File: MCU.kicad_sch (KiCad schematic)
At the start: 33 parts, among them J1 Conn_ARM_SWD_TagConnect_TC2030, U1 STM32WB55CGUx, U2 FM24CL16B, U3 MLPF-WB55-01E3, X1 32MHz, X2 32kHz768

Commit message: Added test points and other cleanup
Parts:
- C14, C15: value C -> 10pF
- TP1, TP2: footprint (none) -> TestPoint:TestPoint_Pad_D1.0mm
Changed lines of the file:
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@@
 	)
 	(junction
+		(at 36.83 31.75)
+		(diameter 0)
+		(color 0 0 0 0)
+	)
+	(junction
 		(at 78.74 21.59)
 		(diameter 0)
@@
 	)
 	(junction
-		(at 101.6 67.31)
-		(diameter 0)
-		(color 0 0 0 0)
-	)
-	(junction
-		(at 34.29 31.75)
-		(diameter 0)
-		(color 0 0 0 0)
-	)
-	(junction
 		(at 133.35 49.53)
 		(diameter 0)
@@
 	)
 	(junction
-		(at 138.43 142.24)
+		(at 101.6 67.31)
 		(diameter 0)
 		(color 0 0 0 0)
 	)
 	(junction
-		(at 106.68 106.68)
+		(at 138.43 142.24)
 		(diameter 0)
 		(color 0 0 0 0)
 	)
 	(junction
-		(at 45.72 21.59)
+		(at 106.68 106.68)
 		(diameter 0)
 		(color 0 0 0 0)
@@
 	(wire
 		(pts
-			(xy 40.64 21.59) (xy 45.72 21.59)
-		)
-		(stroke
-			(width 0)
-			(type default)
-		)
-	)
-	(wire
-		(pts
-			(xy 69.85 69.85) (xy 115.57 69.85)
+			(xy 36.83 31.75) (xy 40.64 31.75)
 		)
 		(stroke
@@
 	(wire
 		(pts
-			(xy 101.6 67.31) (xy 115.57 67.31)
+			(xy 40.64 21.59) (xy 53.34 21.59)
 		)
 		(stroke
@@
 	(wire
 		(pts
-			(xy 45.72 21.59) (xy 53.34 21.59)
+			(xy 130.81 49.53) (xy 124.46 49.53)
 		)
 		(stroke
@@
 	(wire
 		(pts
-			(xy 130.81 49.53) (xy 124.46 49.53)
+			(xy 106.68 106.68) (xy 106.68 109.22)
 		)
 		(stroke
@@
 	(wire
 		(pts
-			(xy 106.68 106.68) (xy 106.68 109.22)
+			(xy 161.29 95.25) (xy 208.28 95.25)
 		)
 		(stroke
@@
 	(wire
 		(pts
-			(xy 161.29 95.25) (xy 208.28 95.25)
+			(xy 163.83 39.37) (xy 163.83 38.1)
 		)
 		(stroke
@@
 	(wire
 		(pts
-			(xy 163.83 39.37) (xy 163.83 38.1)
+			(xy 27.94 20.32) (xy 27.94 21.59)
 		)
 		(stroke
@@
 	(wire
 		(pts
-			(xy 27.94 20.32) (xy 27.94 21.59)
+			(xy 161.29 123.19) (xy 171.45 123.19)
 		)
 		(stroke
@@
 	(wire
 		(pts
-			(xy 161.29 123.19) (xy 171.45 123.19)
+			(xy 46.99 107.95) (xy 46.99 116.84)
 		)
 		(stroke
@@
 	(wire
 		(pts
-			(xy 46.99 107.95) (xy 46.99 116.84)
+			(xy 101.6 67.31) (xy 115.57 67.31)
 		)
 		(stroke
@@
 	(wire
 		(pts
-			(xy 27.94 31.75) (xy 34.29 31.75)
+			(xy 27.94 31.75) (xy 36.83 31.75)
 		)
 		(stroke
@@
 	(wire
 		(pts
-			(xy 34.29 31.75) (xy 40.64 31.75)
-		)
-		(stroke
-			(width 0)
-			(type default)
-		)
-	)
-	(wire
-		(pts
 			(xy 27.94 21.59) (xy 40.64 21.59)
 		)
@@
 	(wire
 		(pts
+			(xy 69.85 69.85) (xy 115.57 69.85)
+		)
+		(stroke
+			(width 0)
+			(type default)
+		)
+	)
+	(wire
+		(pts
 			(xy 138.43 135.89) (xy 138.43 142.24)
 		)
@@
 	)
 	(symbol
-		(lib_id "power:PWR_FLAG")
-		(at 45.72 21.59 0)
-		(unit 1)
-		(exclude_from_sim no)
-		(in_bom yes)
-		(on_board yes)
-		(dnp no)
-		(property "Reference" "#FLG02"
-			(at 45.72 19.685 0)
-			(effects
-				(font
-					(size 1.27 1.27)
-				)
-				(hide yes)
-			)
-		)
-		(property "Value" "PWR_FLAG"
-			(at 45.72 17.78 0)
-			(effects
-				(font
-					(size 0.762 0.762)
-				)
-			)
-		)
-		(property "Footprint" ""
-			(at 45.72 21.59 0)
-			(effects
-				(font
-					(size 1.27 1.27)
-				)
-				(hide yes)
-			)
-		)
-		(property "Datasheet" "~"
-			(at 45.72 21.59 0)
-			(effects
-				(font
-					(size 1.27 1.27)
-				)
-				(hide yes)
-			)
-		)
-		(property "Description" "Special symbol for telling ERC where power comes from"
-			(at 45.72 21.59 0)
-			(effects
-				(font
-					(size 1.27 1.27)
-				)
-				(hide yes)
-			)
-		)
-		(pin "1"
-		)
-		(instances
-			(project "2tonewatch"
-				(path "/29eb74dc-e91c-4cc5-ad9f-7f8caf36d690/d7e41c0d-036e-4359-ac6b-2548c136f4e0"
-					(reference "#FLG02")
-					(unit 1)
-				)
-			)
-		)
-	)
-	(symbol
 		(lib_id "power:GND")
 		(at 105.41 172.72 0)
@@
 			)
 		)
-		(property "Footprint" ""
+		(property "Footprint" "TestPoint:TestPoint_Pad_D1.0mm"
 			(at 107.95 90.17 0)
 			(effects
@@
 		(dnp no)
 		(property "Reference" "C14"
-			(at 89.408 115.57 0)
+			(at 89.662 110.49 0)
 			(effects
 				(font
@@
 			)
 		)
-		(property "Value" "C"
-			(at 95.758 115.316 0)
+		(property "Value" "10pF"
+			(at 88.392 115.316 0)
 			(effects
 				(font
@@
 			)
 		)
-		(property "Footprint" ""
+		(property "Footprint" "TestPoint:TestPoint_Pad_D1.0mm"
 			(at 163.83 67.31 0)
 			(effects
@@
 	)
 	(symbol
+		(lib_id "power:PWR_FLAG")
+		(at 101.6 67.31 0)
+		(unit 1)
+		(exclude_from_sim no)
+		(in_bom yes)
+		(on_board yes)
+		(dnp no)
+		(property "Reference" "#FLG03"
+			(at 101.6 65.405 0)
+			(effects
+				(font
+					(size 1.27 1.27)
+				)
+				(hide yes)
+			)
+		)
+		(property "Value" "PWR_FLAG"
+			(at 101.6 63.5 0)
+			(effects
+				(font
+					(size 0.762 0.762)
+				)
+				(hide yes)
+			)
+		)
+		(property "Footprint" ""
+			(at 101.6 67.31 0)
+			(effects
+				(font
+					(size 1.27 1.27)
+				)
+				(hide yes)
+			)
+		)
+		(property "Datasheet" "~"
+			(at 101.6 67.31 0)
+			(effects
+				(font
+					(size 1.27 1.27)
+				)
+				(hide yes)
+			)
+		)
+		(property "Description" "Special symbol for telling ERC where power comes from"
+			(at 101.6 67.31 0)
+			(effects
+				(font
+					(size 1.27 1.27)
+				)
+				(hide yes)
+			)
+		)
+		(pin "1"
+		)
+		(instances
+			(project "2tonewatch"
+				(path "/29eb74dc-e91c-4cc5-ad9f-7f8caf36d690/d7e41c0d-036e-4359-ac6b-2548c136f4e0"
+					(reference "#FLG03")
+					(unit 1)
+				)
+			)
+		)
+	)
+	(symbol
 		(lib_id "power:GND")
 		(at 60.96 118.11 0)
@@
 		(dnp no)
 		(property "Reference" "C15"
-			(at 102.362 115.316 0)
+			(at 107.188 110.744 0)
 			(effects
 				(font
@@
 			)
 		)
-		(property "Value" "C"
-			(at 108.458 115.316 0)
+		(property "Value" "10pF"
+			(at 107.442 115.316 0)
 			(effects
 				(font
@@
 	(symbol
 		(lib_id "power:PWR_FLAG")
-		(at 34.29 31.75 180)
+		(at 36.83 31.75 0)
 		(unit 1)
 		(exclude_from_sim no)
@@
 		(dnp no)
 		(property "Reference" "#FLG04"
-			(at 34.29 33.655 0)
+			(at 36.83 29.845 0)
 			(effects
 				(font
@@
 		)
 		(property "Value" "PWR_FLAG"
-			(at 34.29 35.56 0)
+			(at 36.83 27.94 0)
 			(effects
 				(font
 					(size 0.762 0.762)
 				)
+				(hide yes)
 			)
 		)
 		(property "Footprint" ""
-			(at 34.29 31.75 0)
+			(at 36.83 31.75 0)
 			(effects
 				(font
@@
 		)
 		(property "Datasheet" "~"
-			(at 34.29 31.75 0)
+			(at 36.83 31.75 0)
 			(effects
 				(font
@@
 		)
 		(property "Description" "Special symbol for telling ERC where power comes from"
-			(at 34.29 31.75 0)
+			(at 36.83 31.75 0)
 			(effects
 				(font
@@
 					(unit 1)
 				)
-			)
-		)
-	)
-	(symbol
-		(lib_id "power:PWR_FLAG")
-		(at 101.6 67.31 0)
-		(unit 1)
-		(exclude_from_sim no)
-		(in_bom yes)
-		(on_board yes)
-		(dnp no)
-		(property "Reference" "#FLG03"
-			(at 101.6 65.405 0)
-			(effects
-				(font
-					(size 1.27 1.27)
-				)
-				(hide yes)
-			)
-		)
-		(property "Value" "PWR_FLAG"
-			(at 101.6 63.5 0)
-			(effects
-				(font
-					(size 0.762 0.762)
-				)
-			)
-		)
-		(property "Footprint" ""
-			(at 101.6 67.31 0)
-			(effects
-				(font
-					(size 1.27 1.27)
-				)
-				(hide yes)
-			)
-		)
-		(property "Datasheet" "~"
-			(at 101.6 67.31 0)
-			(effects
-				(font
-					(size 1.27 1.27)
-				)
-				(hide yes)
-			)
-		)
-		(property "Description" "Special symbol for telling ERC where power comes from"
-			(at 101.6 67.31 0)
-			(effects
-				(font
-					(size 1.27 1.27)
-				)
-				(hide yes)
-			)
-		)
-		(pin "1"
-		)
-		(instances
-			(project "2tonewatch"
-				(path "/29eb74dc-e91c-4cc5-ad9f-7f8caf36d690/d7e41c0d-036e-4359-ac6b-2548c136f4e0"
-					(reference "#FLG03")
-					(unit 1)
-				)

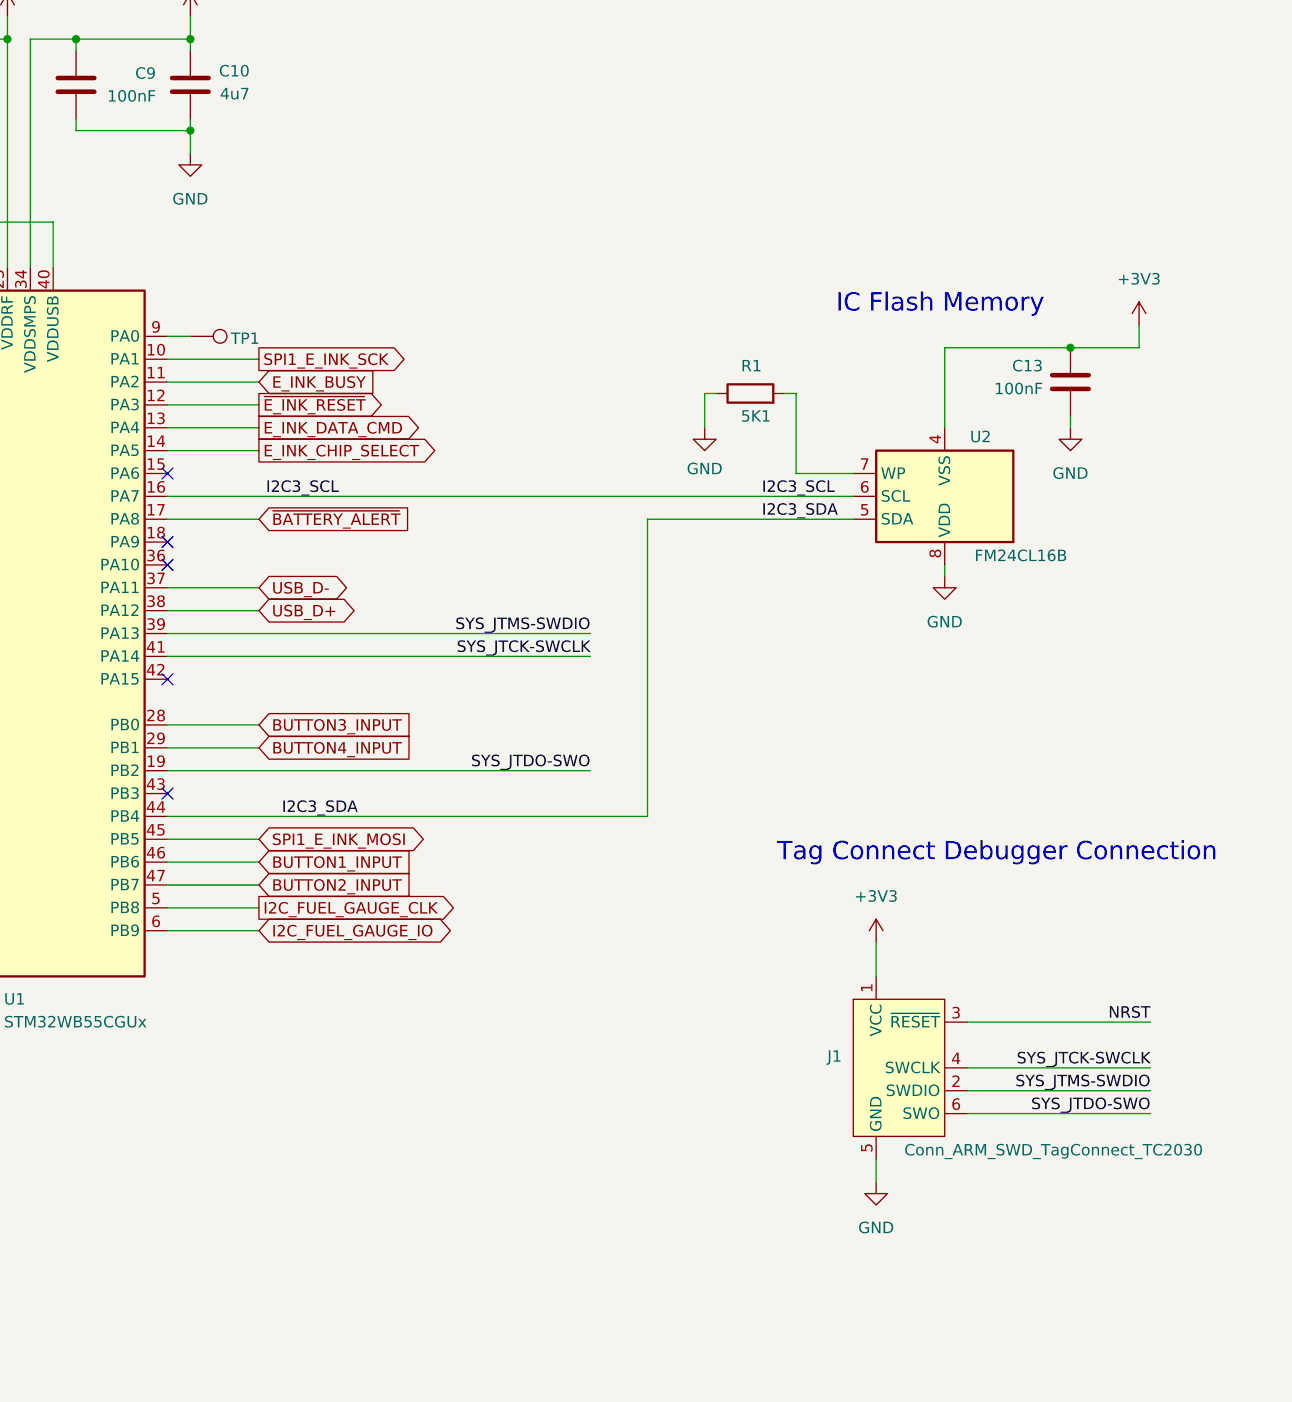
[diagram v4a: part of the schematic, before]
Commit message: changed fram for ic flash memory
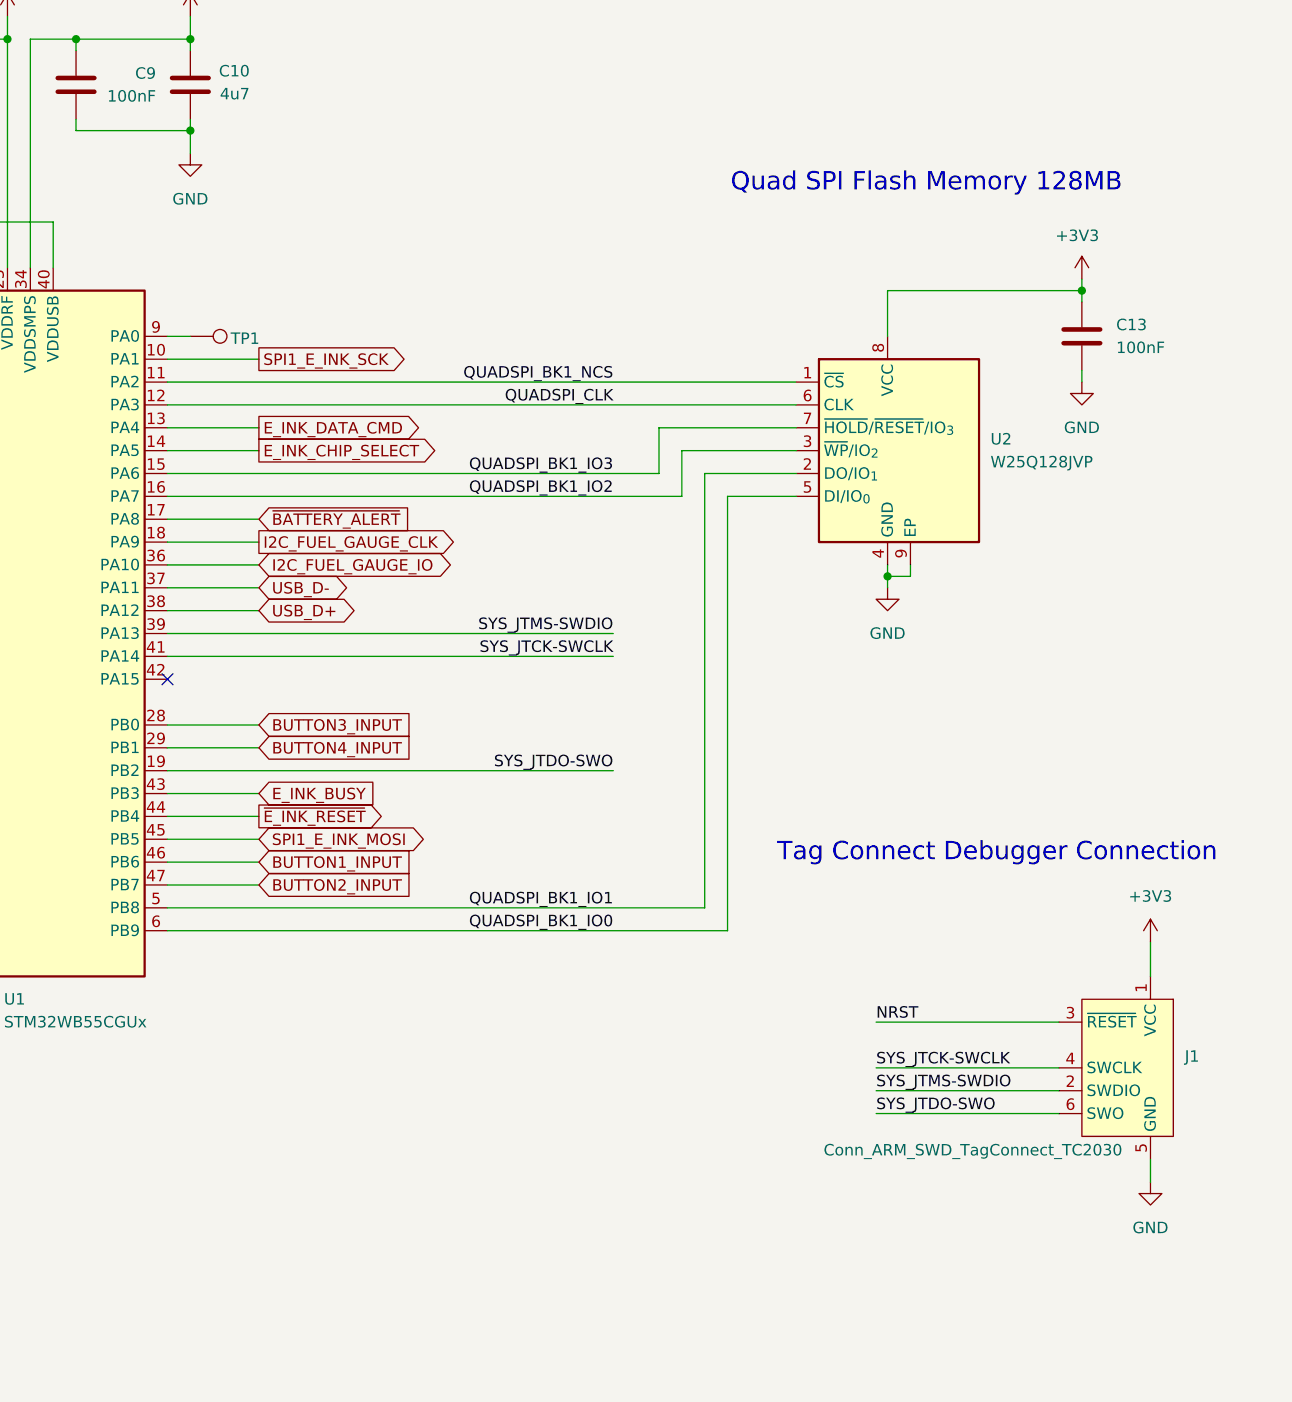
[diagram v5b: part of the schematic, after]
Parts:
- removed R1: 5K1, symbol Device:R
- removed U2: FM24CL16B, Package_SO:SOIC-8_3.9x4.9mm_P1.27mm, symbol Memory_NVRAM:FM24CL16B
- added U2: W25Q128JVP, Package_SON:WSON-8-1EP_6x5mm_P1.27mm_EP3.4x4.3mm, symbol Memory_Flash:W25Q128JVP
- C11, C13, C2, C3, C4, C5, C6, C7, C8, C9: footprint (none) -> Capacitor_SMD:C_0402_1005Metric
- R4: footprint (none) -> Resistor_SMD:R_0402_1005Metric
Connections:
- net I2C3_SDA is gone; now on net ~{E_INK_RESET}: U1.44 (PB4)
- net +3V3: now also U2.8 (VCC)
- net E_INK_BUSY: now also U1.43 (PB3); no longer U1.11 (PA2)
- net GND: now also U2.4 (GND), U2.9 (EP)
- net I2C_FUEL_GAUGE_CLK: now also U1.18 (PA9); no longer U1.5 (PB8)
- net I2C_FUEL_GAUGE_IO: now also U1.36 (PA10); no longer U1.6 (PB9)
- net ~{E_INK_RESET}: no longer U1.12 (PA3)
- net QUADSPI_BK1_IO3: now reaches U1.15 (PA6)
- net QUADSPI_BK1_IO3: now also U2.7 (~{HOLD}/~{RESET}/IO_{3})
- net I2C3_SCL renamed QUADSPI_BK1_IO2
- net QUADSPI_BK1_IO2: now also U2.3 (~{WP}/IO_{2})
- new net QUADSPI_BK1_IO0: U1.6 (PB9), U2.5 (DI/IO_{0})
- new net QUADSPI_BK1_IO1: U1.5 (PB8), U2.2 (DO/IO_{1})
- new net QUADSPI_BK1_NCS: U1.11 (PA2), U2.1 (~{CS})
- new net QUADSPI_CLK: U1.12 (PA3), U2.6 (CLK)
- no-connect marks 5 -> 1
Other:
- note added: "Quad SPI Flash Memory 128MB"
- note removed: "IC Flash Memory"
- moved on the sheet: J1
